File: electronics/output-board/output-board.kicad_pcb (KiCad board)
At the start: 4 copper layers, 113.2 x 84.1 mm, 125 parts, among them J1 Conn_01x02_Male, J10 Conn_01x02_Male, J11 Conn_01x02_Male, J12 Conn_01x02_Male, J13 Conn_01x02_Male, J14 Arming switch, J15 Conn_01x02_Male, J16 Conn_01x02_Male, J17 Conn_01x02_Male, J18 Conn_01x02_Male, J19 Extra IO, J2 Conn_01x02_Male, J20 Ignition Detector, J3 12V In, J4 Conn_01x02, J5 SWD Header, J6 Conn_01x02, J7 Conn_01x02_Male, J8 Conn_01x02_Male, J9 Conn_01x02_Male, SW1 SW_Push_Dual, U1 MAX33014EATB+, U2 LD3985M33R_SOT23, U3 STM32F105VBH6, Y1 36MHz 9pF

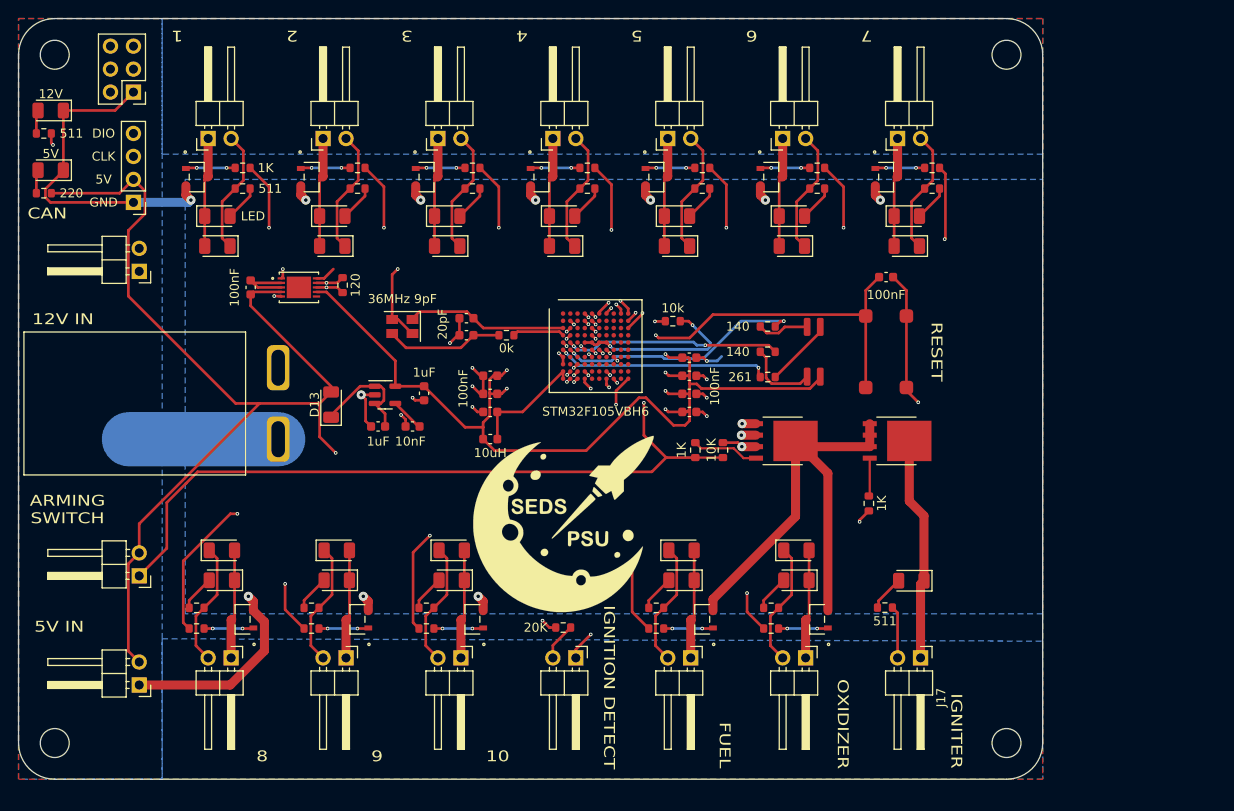
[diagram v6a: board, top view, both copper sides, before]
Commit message: Moved Diodes closer to connectors
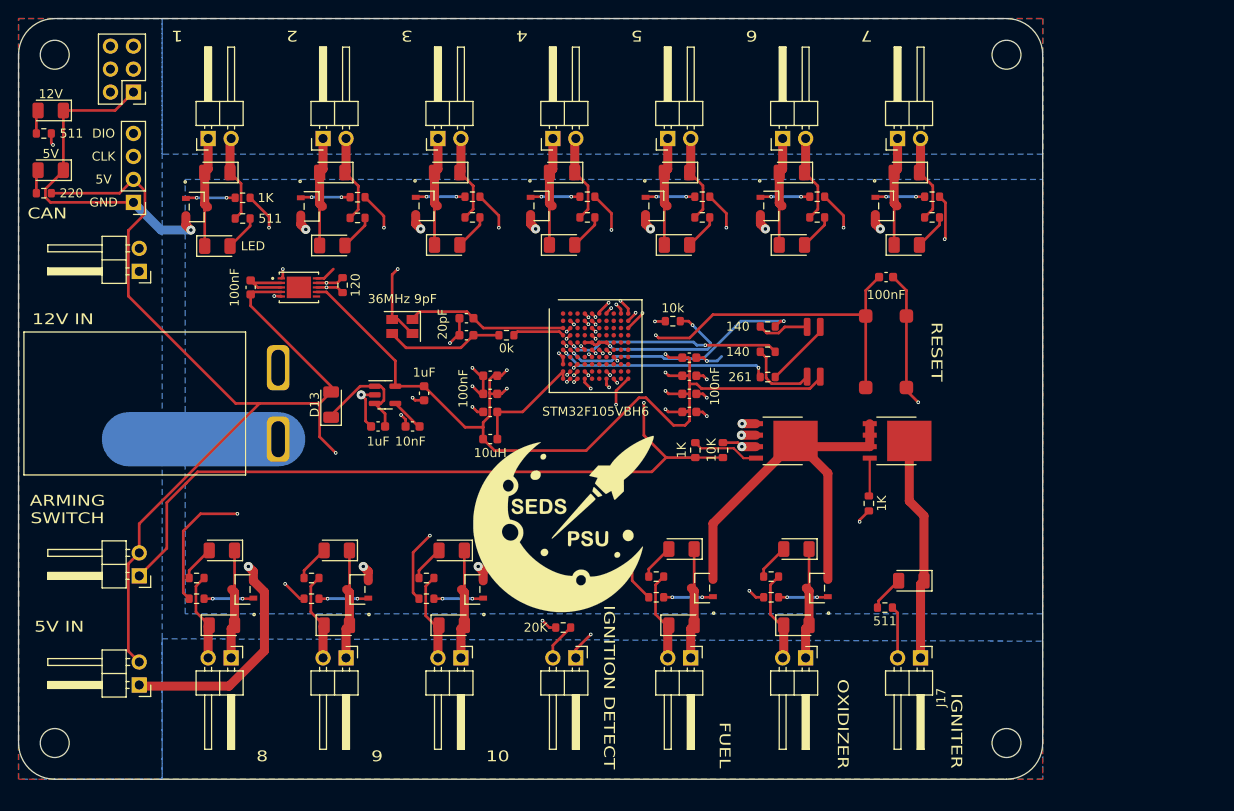
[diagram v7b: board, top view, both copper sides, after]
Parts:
- moved D17 8.28 mm to (49.4, 96.5)
- moved D25 8.28 mm to (74.8, 96.5)
- moved D26 8.28 mm to (62.1, 96.5)
- moved D27 8.28 mm to (100.2, 96.5)
- moved D28 8.28 mm to (112.9, 96.5)
- moved D18 8.13 mm to (48.9, 46.5)
- moved D19 8.13 mm to (61.6, 46.5)
- moved D20 8.13 mm to (74.3, 46.5)
- moved D21 8.13 mm to (87.0, 46.5)
- moved D22 8.13 mm to (99.7, 46.5)
- moved D23 8.13 mm to (112.4, 46.5)
- moved D24 8.13 mm to (125.1, 46.5)
- moved D11 3.45 mm to (100.2, 88.1)
- moved D12 3.45 mm to (112.9, 88.1)
- moved MOSFET11 3.45 mm to (102.5, 92.4)
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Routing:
- net +12V: track 189.0 -> 142.0 mm
- net /MOSFET-sheet10/GROUND: track 53.8 -> 46.9 mm
- net GND: track 160.8 -> 165.5 mm
- net /MOSFET-sheet10/INPUT: track 30.3 -> 26.9 mm
- net /MOSFET-sheet1/INPUT: track 53.1 -> 49.8 mm
- net /MOSFET-sheet8/INPUT: track 46.2 -> 42.9 mm
- net /MOSFET-sheet2/INPUT: track 36.7 -> 33.4 mm
- net /MOSFET-sheet7/INPUT: track 50.9 -> 47.7 mm
- net /MOSFET-sheet6/INPUT: track 43.3 -> 40.1 mm
- net /MOSFET-sheet5/INPUT: track 27.6 -> 24.4 mm
- net /MOSFET-sheet3/INPUT: track 24.4 -> 21.2 mm
- net /MOSFET-sheet4/INPUT: track 17.4 -> 14.2 mm
- net /MOSFET-sheet11/INPUT: track 35.0 -> 31.9 mm
- net /MOSFET-sheet9/INPUT: track 57.1 -> 54.0 mm
- net /MOSFET-sheet/INPUT: track 62.2 -> 60.8 mm

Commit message: Added hole locations for output-board
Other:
- board text added: "105.195 mm"
- board text added: "76.074 mm"
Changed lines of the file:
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@@
     (fp_circle (center 0 0) (end 3.2 0) (layer "Cmts.User") (width 0.15) (fill none))
     (fp_circle (center 0 0) (end 3.45 0) (layer "F.CrtYd") (width 0.05) (fill none))
-    (pad "" np_thru_hole circle (at 0 0) (size 3.2 3.2) (drill 3.2) (layers *.Cu *.Mask))
+    (pad "" np_thru_hole circle (at 0 0) (size 3.2 3.2) (drill 3.2) (layers F&B.Cu *.Mask))
   )
   (footprint "Capacitor_SMD:C_0603_1608Metric" (layer "F.Cu")
@@
   (gr_line (start 136.119 113.538) (end 30.924 113.538) (layer "Edge.Cuts") (width 0.1))
   (gr_line (start 26.924 109.538) (end 26.924 33.464) (layer "Edge.Cuts") (width 0.1))
+  (gr_line (start 30.924 109.538) (end 20.924 109.538) (layer "User.2") (width 0.15))
+  (gr_line (start 30.924 33.464) (end 30.924 23.464) (layer "User.2") (width 0.15))
+  (gr_line (start 30.924 33.464) (end 20.924 33.464) (layer "User.2") (width 0.15))
+  (gr_line (start 31 25) (end 136 25) (layer "User.2") (width 0.15))
+  (gr_line (start 22.75 33.5) (end 22.75 109.5) (layer "User.2") (width 0.15))
+  (gr_line (start 136.119 33.464) (end 136.119 23.464) (layer "User.2") (width 0.15))
   (gr_text "4" (at 82.55 31.369 180) (layer "F.SilkS")
     (effects (font (size 1.2 1.5) (thickness 0.3)))
@@
     (effects (font (size 1.2 1.5) (thickness 0.3)))
   )
+  (gr_text "76.074 mm" (at 19.25 71.75 90) (layer "User.2")
+    (effects (font (size 2 2) (thickness 0.3)))
+  )
+  (gr_text "105.195 mm" (at 91.75 22.75) (layer "User.2")
+    (effects (font (size 2 2) (thickness 0.3)))
+  )
   (segment (start 46.52852 92.199387) (end 46.52852 95.05052) (width 0.3) (layer "F.Cu") (net 1))
